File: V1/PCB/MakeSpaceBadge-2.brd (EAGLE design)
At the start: 97.5 x 91.5 mm, 67 parts

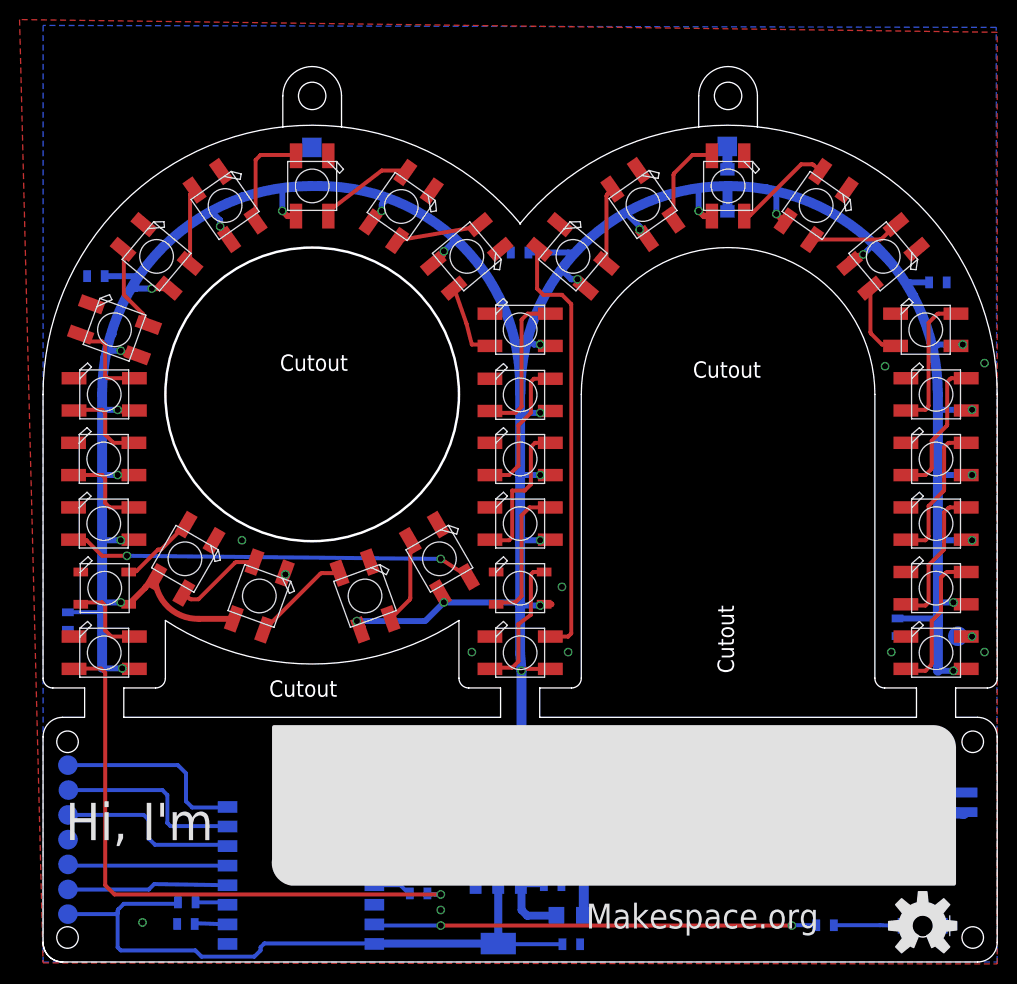
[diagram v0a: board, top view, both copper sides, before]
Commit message: Added notes.
Added mini case to hold battery/protect electronics.

Added firmware to drive leds.
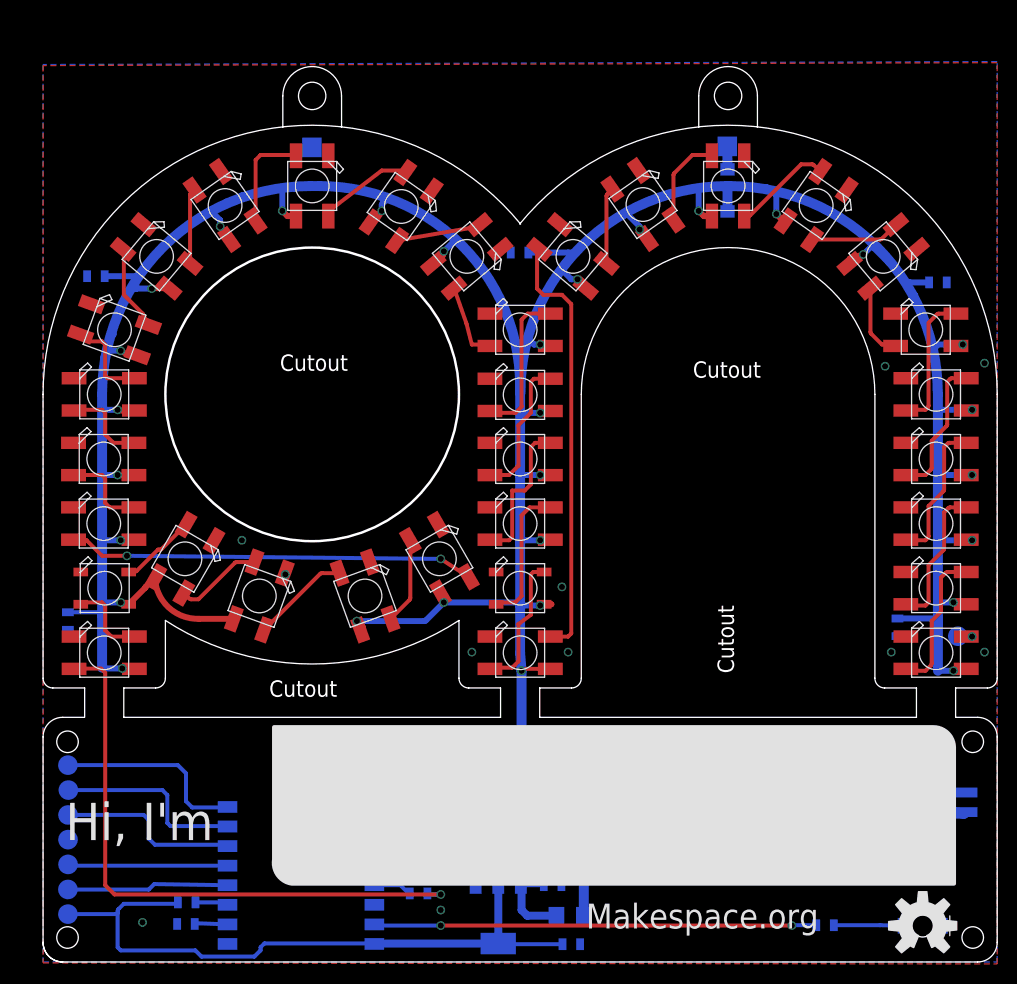
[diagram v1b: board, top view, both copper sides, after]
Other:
- board text added: "0"
- board text added: "1"
- board text added: "10"
- board text added: "11"
- board text added: "12"
- board text added: "13"
- board text added: "14"
- board text added: "15"
- board text added: "16"
- board text added: "17"
- board text added: "18"
- board text added: "19"
- board text added: "2"
- board text added: "20"
- board text added: "21"
- board text added: "22"
- board text added: "23"
- board text added: "24"
- board text added: "25"
- board text added: "26"
- board text added: "27"
- board text added: "28"
- board text added: "29"
- board text added: "3"
- board text added: "30"
- board text added: "31"
- board text added: "4"
- board text added: "5"
- board text added: "6"
- board text added: "7"
- board text added: "8"
- board text added: "9"
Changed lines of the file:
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@@
 <layer number="45" name="Holes" color="7" fill="1" visible="yes" active="yes"/>
 <layer number="46" name="Milling" color="3" fill="1" visible="no" active="yes"/>
-<layer number="47" name="Measures" color="7" fill="1" visible="yes" active="yes"/>
+<layer number="47" name="Measures" color="7" fill="1" visible="no" active="yes"/>
 <layer number="48" name="Document" color="7" fill="1" visible="yes" active="yes"/>
 <layer number="49" name="Reference" color="13" fill="1" visible="yes" active="yes"/>
@@
 <wire x1="24.5" y1="150.5" x2="30.5" y2="150.5" width="0" layer="20" curve="-180"/>
 <wire x1="67" y1="150.5" x2="73" y2="150.5" width="0" layer="20" curve="-180"/>
+<dimension x1="2.5" y1="64.5" x2="0" y2="64.5" x3="1.25" y3="60.3" textsize="1.016" layer="47"/>
+<dimension x1="0" y1="85" x2="18.3" y2="84.6" x3="9.15" y3="87.6" textsize="1.016" layer="47" dtype="horizontal"/>
+<dimension x1="0" y1="85" x2="34.4" y2="85.8" x3="17.2" y3="87.6" textsize="1.016" layer="47" dtype="horizontal"/>
+<dimension x1="2" y1="62" x2="27.5" y2="153.5" x3="-35.8" y3="107.75" textsize="1.016" layer="47" dtype="vertical"/>
+<text x="5.7" y="92.9" size="1.778" layer="49">0</text>
+<text x="5.8" y="99.4" size="1.778" layer="49">1</text>
+<text x="14" y="102.4" size="1.778" layer="49">2</text>
+<text x="21.6" y="98.6" size="1.778" layer="49">3</text>
+<text x="32.2" y="98.4" size="1.778" layer="49">4</text>
+<text x="39.9" y="102.4" size="1.778" layer="49">5</text>
+<text x="5.4" y="105.9" size="1.778" layer="49">6</text>
+<text x="5.8" y="112.6" size="1.778" layer="49">7</text>
+<text x="5.5" y="119.1" size="1.778" layer="49">8</text>
+<text x="6.6" y="125.8" size="1.778" layer="49">9</text>
+<text x="10.2" y="133.3" size="1.778" layer="49">10</text>
+<text x="17.4" y="138.6" size="1.778" layer="49">11</text>
+<text x="26.1" y="140.5" size="1.778" layer="49">12</text>
+<text x="35.2" y="138.4" size="1.778" layer="49">13</text>
+<text x="41.9" y="133.3" size="1.778" layer="49">14</text>
+<text x="47.4" y="125.8" size="1.778" layer="49">15</text>
+<text x="47.5" y="119.2" size="1.778" layer="49">16</text>
+<text x="47.4" y="112.5" size="1.778" layer="49">17</text>
+<text x="47.4" y="105.9" size="1.778" layer="49">18</text>
+<text x="47.4" y="99.4" size="1.778" layer="49">19</text>
+<text x="47.4" y="92.8" size="1.778" layer="49">20</text>
+<text x="52.9" y="133.4" size="1.778" layer="49">21</text>
+<text x="59.9" y="138.6" size="1.778" layer="49">22</text>
+<text x="68.6" y="140.5" size="1.778" layer="49">23</text>
+<text x="77.7" y="138.5" size="1.778" layer="49">24</text>
+<text x="84.4" y="133.2" size="1.778" layer="49">25</text>
+<text x="88.9" y="125.7" size="1.778" layer="49">26</text>
+<text x="89.9" y="119.1" size="1.778" layer="49">27</text>
+<text x="89.9" y="112.6" size="1.778" layer="49">28</text>
+<text x="89.9" y="106" size="1.778" layer="49">29</text>
+<text x="89.8" y="99.4" size="1.778" layer="49">30</text>
+<text x="90" y="92.8" size="1.778" layer="49">31</text>
 </plain>
 <attributes>
@@
 <vertex x="0" y="62"/>
 <vertex x="97.5" y="62"/>
-<vertex x="97.4" y="157.5"/>
-<vertex x="0" y="157.7"/>
+<vertex x="97.5" y="154"/>
+<vertex x="0" y="153.7"/>
 </polygon>
 <polygon width="0.4064" layer="1">
 <vertex x="0" y="61.9"/>
 <vertex x="97.5" y="61.8"/>
-<vertex x="97.5" y="157"/>
-<vertex x="-2.4" y="158.3"/>
-<vertex x="0" y="62"/>
+<vertex x="97.5" y="153.9"/>
+<vertex x="0" y="153.6"/>
 </polygon>
 <contactref element="GND" pad="TP"/>
